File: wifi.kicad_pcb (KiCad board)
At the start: 4 copper layers, 58.4 x 69.6 mm, 134 parts, among them J1 Conn_02x10_Odd_Even, J11 Conn_Coaxial, J12 Conn_02x05_Counter_Clockwise, J13 Conn_02x03_Odd_Even, J14 Conn_01x02, J15 Conn_01x02, J16 Conn_01x02, J2 Conn_02x10_Odd_Even, J21 Conn_02x04_Odd_Even, J22 Conn_01x03, J23 Conn_01x03, J24 Conn_01x02, J3 Conn_02x06_Odd_Even, J5 Conn_01x03, J6 Conn_01x03, J7 Conn_02x07_Odd_Even, J9 Conn_01x02, Q2 TP0610T, Q3 BSS138, Q4 BSS138, Q5 BSS138, SW2 SW_DIP_x01, SW3 SW_DIP_x01, U1 CC3220SM2ARGKT, U10 TMP100, U8 MX25R3235FM1IL0, U9 OPA4340UA, Y2 32.768kHz, Y3 Crystal_GND24_Small

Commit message: Fixes for Aisler
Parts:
- added FID1: Fiducial, Fiducial:Fiducial_0.5mm_Mask1mm, F.Cu at (127.4, 51.8)
- added FID2: Fiducial, Fiducial:Fiducial_0.5mm_Mask1mm, F.Cu at (132.3, 110.9)
- added FID3: Fiducial, Fiducial:Fiducial_0.5mm_Mask1mm, F.Cu at (82.7, 52.2)
- added R45: 0, Resistor_SMD:R_0402_1005Metric, F.Cu at (79.1, 93.8)
- added R75: 0, Resistor_SMD:R_0402_1005Metric, F.Cu at (79.2, 85.3)
- added R78: 0, Resistor_SMD:R_0402_1005Metric, F.Cu at (131.3, 92.7)
- added R81: 0, Resistor_SMD:R_0402_1005Metric, F.Cu at (123.5, 95.2)
- added R85: 0, Resistor_SMD:R_0402_1005Metric, F.Cu at (123.6, 97.8)
- added R89: 0, Resistor_SMD:R_0402_1005Metric, F.Cu at (79.1, 95.5)
- added R91: 0, Resistor_SMD:R_0402_1005Metric, F.Cu at (79.1, 98.0)
- C35: footprint Capacitor_SMD:C_0402_1005Metric -> Capacitor_SMD:C_0603_1608Metric
- U1: footprint Package_DFN_QFN:Texas_S-PVQFN-N64_EP4.25x4.25mm -> Package_DFN_QFN:Texas_S-PVQFN-N64_EP4.25x4.25mm_ThermalVias
- moved J21 0.92 mm to (94.7, 54.9)
- moved J3 0.92 mm to (115.1, 54.9)
- moved J5 0.92 mm to (99.9, 57.4)
- moved J6 0.92 mm to (97.3, 57.4)
- moved R87 0.64 mm to (79.1, 92.3)
- moved C50 0.51 mm to (99.3, 95.8)
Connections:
- J1 pad 17: (no net) -> Net-(J1-Pad17)
- J1 pad 19: (no net) -> Net-(J1-Pad19)
- J1 pad 9: (no net) -> Net-(J1-Pad9)
- J2 pad 16: (no net) -> Net-(J2-Pad16)
- J2 pad 17: (no net) -> Net-(J2-Pad17)
- J2 pad 19: (no net) -> Net-(J2-Pad19)
- J2 pad 2: (no net) -> GND
- J3 pad 10: (no net) -> /P20_JTAG_TMS
- J3 pad 4: (no net) -> /P17_GPIO_24
- J3 pad 6: (no net) -> /P16_JTAG_TDI
- J3 pad 8: (no net) -> /P19_JTAG_TCK
- R52 pad 1: (no net) -> /P21_GPIO_25
- U1 pad 16: (no net) -> /P16_JTAG_TDI
- U1 pad 17: (no net) -> /P17_GPIO_24
- U1 pad 19: (no net) -> /P19_JTAG_TCK
- U1 pad 20: (no net) -> /P20_JTAG_TMS
- U1 pad 61: (no net) -> /P61_GPIO_06
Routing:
- net /P17_GPIO_24: track 0.00 -> 88.0 mm, vias 0 -> 4
- net /P16_JTAG_TDI: track 0.00 -> 77.1 mm, vias 0 -> 3
- net /P19_JTAG_TCK: track 0.00 -> 68.4 mm, vias 0 -> 2
- net /P20_JTAG_TMS: track 0.00 -> 68.3 mm, vias 0 -> 2
- net /P16_GPIO_23: track 0.00 -> 52.2 mm, vias 0 -> 2
- net /P61_GPIO_06: track 0.00 -> 35.4 mm, vias 0 -> 2
- net /P55_GPIO_01: track 56.3 -> 33.1 mm
- net /P21_GPIO_25: track 0.00 -> 16.0 mm, vias 0 -> 2
- net (no net): track 7.16 -> 0.00 mm, vias 1 -> 0
- net /ANA_IN2: track 31.9 -> 29.2 mm
- net Net-(J1-Pad19): track 0.00 -> 2.69 mm
- net Net-(J1-Pad17): track 0.00 -> 2.69 mm
- net Net-(J1-Pad9): track 0.00 -> 2.63 mm
- net /VBAT_CC: track 98.5 -> 100.9 mm, vias 8 -> 9
- net Net-(J2-Pad16): track 0.00 -> 2.31 mm
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- added copper zone on B.Cu, net GND
- added copper zone on P.Cu, net GND
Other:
- board text added: "5V"
- board text added: "BRD"
- board text added: "GND"
- board text added: "RST"
- board text added: "RX"
- board text added: "TCK"
- board text added: "TDI"
- board text added: "TDO"
- board text added: "TMS"
- board text added: "TX"
- board text added: "VBAT"
- board text added: "VS"

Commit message: MODASF initial commit
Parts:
- removed AE1: Antenna_Chip, pwrcon:Taiyo_WLAN
- removed the C27 at (113.0, 96.4)
- removed the C28 at (106.5, 77.2)
- removed the C29 at (113.3, 87.1)
- removed C32, C37, C38, C43, C44, C46, C47: 0.1uF, Capacitor_SMD:C_0402_1005Metric
- removed the C33 at (93.2, 81.8)
- removed the C34 at (109.2, 114.4)
- removed the C35 at (117.1, 90.4)
- removed C36: 10uF, Capacitor_SMD:C_0402_1005Metric
- removed C45: 10uF, Capacitor_SMD:C_0603_1608Metric
- removed C48, C49, C50, C51: 6.2pF, Capacitor_SMD:C_0402_1005Metric
- removed FL1: BFCN-2450, pwrcon:TDK_Filter
- removed J11: Conn_Coaxial, pwrcon:Co-axial_Connector_RF
- removed the J14 at (79.2, 58.2)
- removed the J21 at (94.7, 54.9)
- removed L3: L_Core_Ferrite_Small, Inductor_SMD:L_01005_0402Metric
- removed L4, L6: 2.2uH, Inductor_SMD:L_Wuerth_MAPI-2512
- removed L5: 1uH, Inductor_SMD:L_Wuerth_MAPI-2512
- removed R128, R39, R40, R43: 0, Resistor_SMD:R_0402_1005Metric
- removed R30: 1K, Resistor_SMD:R_0402_1005Metric
- removed R35: 10K, Resistor_SMD:R_0402_1005Metric
- removed R36: 0, Resistor_SMD:R_0603_1608Metric
- removed R41: 10k, Resistor_SMD:R_0402_1005Metric
- removed the R49 at (123.8, 67.8)
- removed the R50 at (122.0, 67.8)
- removed R51: 2.7K, Resistor_SMD:R_0402_1005Metric
- removed REF** (x4): MountingHole_2.1mm, MountingHole:MountingHole_2.1mm
- removed U8: MX25R3235FM1IL0, Package_SO:SOIC-8_3.9x4.9mm_P1.27mm
- removed Y2: 32.768kHz, Crystal:Crystal_SMD_3215-2Pin_3.2x1.5mm
- removed Y3: Crystal_GND24_Small, Crystal:Crystal_SMD_2520-4Pin_2.5x2.0mm
- added C41: 100uF, Capacitor_SMD:C_0402_1005Metric, F.Cu at (118.7, 72.9)
- added J10: Conn_01x02, Connector_PinHeader_2.54mm:PinHeader_1x02_P2.54mm_Vertical, F.Cu at (113.9, 105.6)
- added J16: Conn_01x02, Connector_PinHeader_2.54mm:PinHeader_1x02_P2.54mm_Vertical, F.Cu at (86.9, 54.9)
- added J17: Conn_01x02, Connector_PinHeader_2.54mm:PinHeader_1x02_P2.54mm_Vertical, F.Cu at (118.2, 54.9)
- added J18: Conn_01x02, Connector_PinHeader_2.54mm:PinHeader_1x02_P2.54mm_Vertical, F.Cu at (94.2, 54.9)
- added J19: Conn_01x02, Connector_PinHeader_2.54mm:PinHeader_1x02_P2.54mm_Vertical, F.Cu at (91.9, 54.9)
- added J20: Conn_01x02, Connector_PinHeader_2.54mm:PinHeader_1x02_P2.54mm_Vertical, F.Cu at (89.5, 54.9)
- added J22: Conn_01x03, Connector_PinHeader_2.54mm:PinHeader_1x03_P2.54mm_Vertical, F.Cu at (84.9, 110.4)
- added R104: 0, Resistor_SMD:R_0402_1005Metric, F.Cu at (88.1, 99.5)
- added R31: 1K, Resistor_SMD:R_0402_1005Metric, F.Cu at (111.6, 69.0)
- added R42: 0, Resistor_SMD:R_0402_1005Metric, F.Cu at (131.1, 77.7)
- added R46: 0, Resistor_SMD:R_0402_1005Metric, F.Cu at (131.1, 82.2)
- added R52: 0, Resistor_SMD:R_0402_1005Metric, F.Cu at (131.6, 87.6)
- added R56: 0, Resistor_SMD:R_0402_1005Metric, F.Cu at (131.5, 90.2)
- added R65: 0, Resistor_SMD:R_0402_1005Metric, F.Cu at (79.0, 90.4)
- added TP1: TestPoint, TestPoint:TestPoint_Pad_D2.0mm, F.Cu at (115.2, 69.0)
- C33: renamed from C30; value 4.7uF -> 0.1uF
- C34: renamed from C31; value 4.7uF -> 0.1uF
- C42: value 10uF -> 100uF; footprint Capacitor_SMD:C_0603_1608Metric -> Capacitor_SMD:C_0402_1005Metric
- R119: value 3.3K -> 0
- R126: renamed from R118; value 3.3K -> 0
- R145: renamed from R147; value 270 -> 750
- R146: renamed from R148; value 270 -> 750
- R147: renamed from R149; value 270 -> 750
- U1: value CC3220SM2ARGKT -> CC3220MODASF12MONR; footprint Package_DFN_QFN:Texas_S-PVQFN-N64_EP4.25x4.25mm_ThermalVias -> TIMOD_footprints:CC3220MODASF12MONR
- U10: value TMP100 -> TMP006AIYZFR; footprint Package_TO_SOT_SMD:SOT-23-6 -> TMP006_footprints:TMP006AIYZFR
- moved J9 63.3 mm to (79.0, 57.4)
- moved J26 40.0 mm to (121.7, 116.2), turned to 270 degrees
- moved J14 38.4 mm to (116.7, 78.6), turned to 225 degrees
- moved J15 38.2 mm to (112.3, 74.2), turned to 225 degrees
- moved R126 33.1 mm to (109.6, 84.9), turned to 180 degrees
- moved R119 32.8 mm to (106.4, 82.6), turned to 180 degrees
- moved R44 31.5 mm to (131.1, 80.0), turned to 0 degrees
- moved R121 30.9 mm to (113.7, 79.6), turned to 0 degrees
- moved R127 30.3 mm to (107.6, 73.5), turned to 180 degrees
- moved C35 30.0 mm to (106.4, 88.1)
- moved R114 29.9 mm to (107.6, 88.1)
- moved U10 29.4 mm to (106.4, 85.3), turned to 180 degrees
- moved C34 27.2 mm to (115.2, 108.8), turned to 270 degrees
- moved C33 23.1 mm to (113.5, 108.8), turned to 270 degrees
- moved R133 22.9 mm to (103.2, 87.9)
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- renumbered C52 to C26, C53 to C27, C54 to C28, C55 to C29, C56 to C30, C57 to C35, D8 to D7, J12 to J112, J13 to J12, J15 to J14, J16 to J15, J22 to J21, J23 to J26, Q3 to Q4, Q2 to Q5, Q4 to Q6, Q5 to Q7, R45 to R105, R47 to R107, R52 to R109, R53 to R113, R116 to R114, R123 to R121, R129 to R127, R134 to R132, R135 to R133, R136 to R134, R138 to R136, R139 to R137, R141 to R139, R142 to R140, R151 to R149, R152 to R150, R153 to R151, R154 to R152, R57 to R38, R67 to R49, R68 to R50, R71 to R53, R72 to R54, R75 to R57, R76 to R58, R78 to R60, R80 to R62, R81 to R63, R82 to R64, R84 to R66, R85 to R67, R86 to R68, R87 to R69, R88 to R70, R89 to R71, R90 to R72, R91 to R73, R92 to R74, R102 to R84, R103 to R85, R104 to R86, R105 to R87, R106 to R88, R107 to R89, R110 to R92, R111 to R93, R112 to R94, R113 to R95, R114 to R96, R115 to R97
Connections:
- net Net-(J1-Pad5) renamed /RX
- net Net-(J1-Pad7) renamed /TX
- net Net-(J1-Pad9) renamed /GPIO
- C35 pad 2: Net-(C57-Pad2) -> Net-(C35-Pad2)
- C42 pad 2: /VDD_DIG_CC -> /VBAT_CC
- J1 pad 1: Net-(J1-Pad1) -> /PWR
- J1 pad 13: (no net) -> Net-(J1-Pad13)
- J112 pad 10: /SFL_CS -> (no net)
- J112 pad 6: /SFL_DIN -> (no net)
- J112 pad 7: /SFL_DOUT -> (no net)
- J112 pad 8: /SFL_CLK -> (no net)
- J12 pad 1: Net-(J13-Pad1) -> Net-(J12-Pad1)
- J12 pad 3: Net-(J13-Pad1) -> Net-(J12-Pad1)
- J12 pad 5: Net-(J13-Pad1) -> Net-(J12-Pad1)
- J2 pad 12: (no net) -> Net-(J2-Pad12)
- J2 pad 14: (no net) -> Net-(J2-Pad14)
- J2 pad 4: (no net) -> Net-(J2-Pad4)
- J2 pad 6: (no net) -> Net-(J2-Pad6)
- J2 pad 8: (no net) -> Net-(J2-Pad8)
- J26 pad 1: /VCC_5V -> /VCC_BRD
- J26 pad 2: GND -> Net-(J26-Pad2)
- J26 pad 3: GND -> /VBAT_CC
- J3 pad 4: /P17_GPIO_24 -> /P17_JTAG_TDO
- J9 pad 1: Net-(J9-Pad1) -> /VCC_BRD
- J9 pad 2: /VBAT_CC -> /VCC_OPAMP
- R105 pad 1: /P16_GPIO_23 -> /P16_JTAG_TDI
- R105 pad 2: /P16_JTAG_TDI -> /P16_GPIO_23
- R107 pad 1: /VCC_BRD -> Net-(J12-Pad1)
- R107 pad 2: Net-(J13-Pad1) -> Net-(J26-Pad2)
- R114 pad 1: /VCC_BRD -> (no net)
- R114 pad 2: Net-(C57-Pad2) -> Net-(C35-Pad2)
- R119 pad 1: /VCC_BRD -> Net-(R119-Pad1)
- R119 pad 2: /SENS_I2C_SCL -> /VCC_BRD
- R126 pad 1: /SENS_I2C_SDA -> GND
- R126 pad 2: /VCC_BRD -> Net-(R126-Pad2)
- R132 pad 1: Net-(R134-Pad1) -> (no net)
- R132 pad 2: /SENS_I2C_SCL -> (no net)
- R133 pad 1: Net-(R135-Pad1) -> (no net)
- R133 pad 2: /SENS_I2C_SDA -> (no net)
- R38 pad 1: /VCC_BRD -> /PWR
- R38 pad 2: Net-(J1-Pad1) -> /VBAT_CC
- R44 pad 1: Net-(R44-Pad1) -> /P08_GPIO_17
- R44 pad 2: GND -> Net-(J2-Pad6)
- U1 pad 1: /P01_GPIO_10 -> GND
- U1 pad 10: Net-(C28-Pad1) -> /P04_GPIO_13
- U1 pad 11: /SFL_CLK -> /P15_GPIO_22
- U1 pad 12: /SFL_DOUT -> /P16_JTAG_TDI
- U1 pad 13: /SFL_DIN -> (no net)
- U1 pad 14: /SFL_CS -> (no net)
- U1 pad 15: /P15_GPIO_22 -> (no net)
- U1 pad 16: /P16_JTAG_TDI -> GND
- U1 pad 17: /P17_GPIO_24 -> (no net)
- U1 pad 18: (no net) -> /P17_JTAG_TDO
- U1 pad 19: /P19_JTAG_TCK -> /P18_GPIO_28
- U1 pad 2: /P02_GPIO_11 -> GND
- U1 pad 20: /P20_JTAG_TMS -> (no net)
- U1 pad 21: /SOP2 -> /P19_JTAG_TCK
- U1 pad 22: Net-(C50-Pad1) -> /P20_JTAG_TMS
- U1 pad 23: Net-(R44-Pad1) -> /SOP2
- U1 pad 24: /VDD_PL -> /SOP1
- U1 pad 25: /LDO_IN -> (no net)
- U1 pad 27: (no net) -> GND
- U1 pad 28: (no net) -> GND
- U1 pad 3: /P03_GPIO_12 -> /P01_GPIO_10
- U1 pad 30: (no net) -> GND
- U1 pad 31: Net-(FL1-Pad1) -> (no net)
- U1 pad 32: /CC_nRESET -> GND
- U1 pad 34: /SOP1 -> /SOP0
- U1 pad 35: /SOP0 -> (no net)
- U1 pad 36: /LDO_IN -> Net-(J10-Pad1)
- U1 pad 38: Net-(L4-Pad2) -> GND
- U1 pad 39: /VBAT_CC -> (no net)
- U1 pad 4: /P04_GPIO_13 -> /P02_GPIO_11
- U1 pad 40: Net-(L5-Pad1) -> /VBAT_CC
- U1 pad 41: Net-(L5-Pad2) -> (no net)
- U1 pad 42: (no net) -> /P53_GPIO_30
- U1 pad 43: Net-(L6-Pad1) -> GND
- U1 pad 44: /VBAT_CC -> /P50_GPIO_00
- U1 pad 46: (no net) -> /P55_GPIO_01
- U1 pad 47: /VDD_FL -> /P57_GPIO_02
- U1 pad 48: /LDO_IN -> /P58_GPIO_03
- U1 pad 49: Net-(C46-Pad1) -> /P59_GPIO_04
- U1 pad 5: (no net) -> /P05_GPIO_14
- U1 pad 50: /P50_GPIO_00 -> /P60_GPIO_05
- U1 pad 51: Net-(C49-Pad2) -> /P61_GPIO_06
- U1 pad 52: Net-(C48-Pad2) -> /P62_GPIO_07
- U1 pad 53: /P53_GPIO_30 -> /P63_GPIO_08
- U1 pad 54: Net-(C28-Pad1) -> /P64_GPIO_09
- U1 pad 55: /P55_GPIO_01 -> GND
- U1 pad 56: /VDD_DIG_CC -> GND
- U1 pad 57: /P57_GPIO_02 -> GND
- U1 pad 58: /P58_GPIO_03 -> GND
- U1 pad 59: /P59_GPIO_04 -> GND
- U1 pad 6: (no net) -> /P06_GPIO_15
- U1 pad 60: /P60_GPIO_05 -> GND
- U1 pad 61: /P61_GPIO_06 -> GND
- U1 pad 62: /P62_GPIO_07 -> GND
- U1 pad 63: /P63_GPIO_08 -> GND
- U1 pad 7: (no net) -> /P07_GPIO_16
- U1 pad 8: (no net) -> /P08_GPIO_17
- U1 pad 9: /VDD_DIG_CC -> /P03_GPIO_12
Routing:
- net /VCC_BRD: track 196.3 -> 37.5 mm, vias 10 -> 6
- net /P01_GPIO_10: track 125.4 -> 1.86 mm, vias 7 -> 0
- net /P02_GPIO_11: track 119.9 -> 1.99 mm, vias 7 -> 0
- net /VBAT_CC: track 100.9 -> 6.39 mm, vias 9 -> 1
- net /P17_GPIO_24: track 88.0 -> 0.28 mm, vias 4 -> 0
- net /P64_GPIO_09: track 81.0 -> 3.19 mm, vias 3 -> 1
- net /P50_GPIO_00: track 77.1 -> 0.00 mm, vias 5 -> 0
- net /P16_JTAG_TDI: track 77.1 -> 0.44 mm, vias 3 -> 0
- net /P19_JTAG_TCK: track 68.4 -> 0.00 mm, vias 2 -> 0
- net /P20_JTAG_TMS: track 68.3 -> 0.00 mm, vias 2 -> 0
- net GND: track 80.6 -> 16.0 mm, vias 38 -> 4
- net /VCC_5V: track 62.8 -> 0.00 mm
- net /SOP2: track 62.1 -> 0.00 mm, vias 2 -> 0
- net /CC_nRESET: track 104.1 -> 49.5 mm, vias 4 -> 2
- net /P16_GPIO_23: track 52.2 -> 1.09 mm, vias 2 -> 1
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- removed copper zone on P.Cu, net /LDO_IN
- removed copper zone on P.Cu, net /VBAT_CC
- removed copper zone on P.Cu, net /VCC_BRD
- removed copper zone on B.Cu, net GND
- removed copper zone on F.Cu, net GND
- removed copper zone on G.Cu, net GND
- removed copper zone on P.Cu, net GND

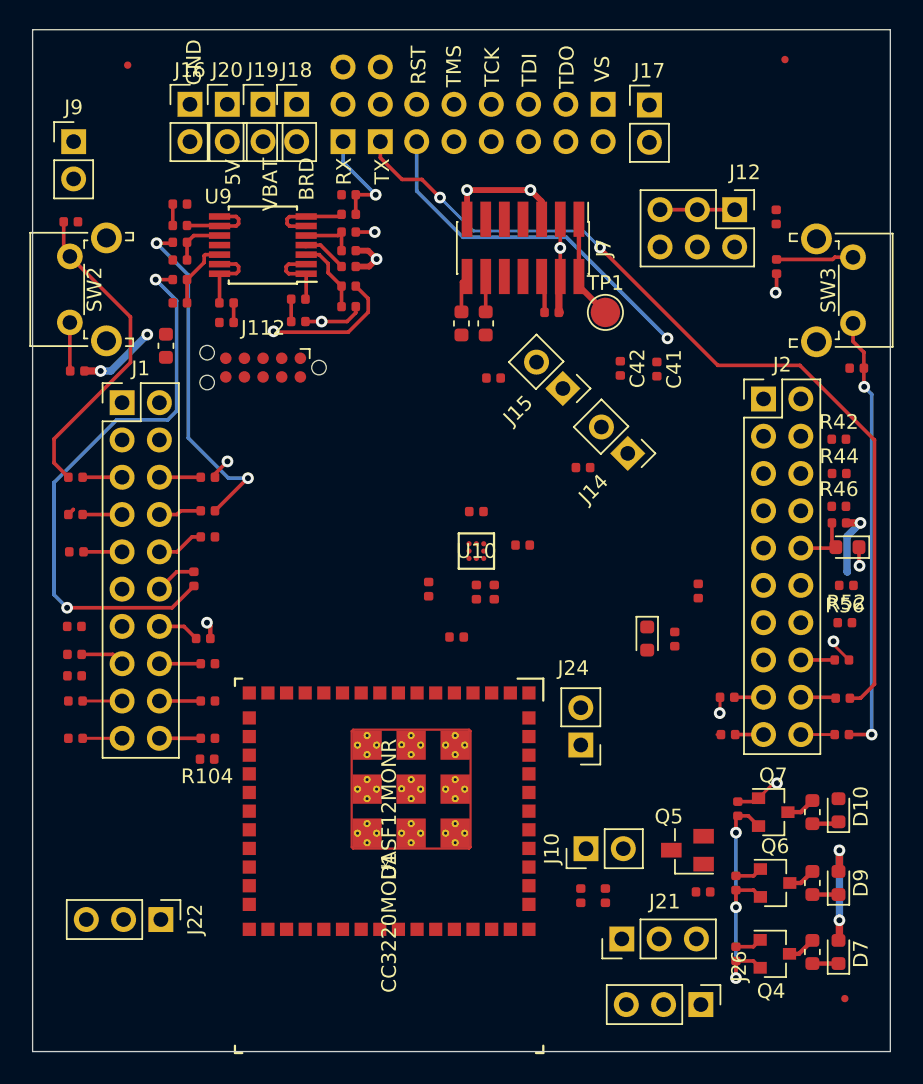
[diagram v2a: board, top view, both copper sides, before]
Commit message: Updated BoM, decided to use 3 LEDs and switches from cc3220s layout
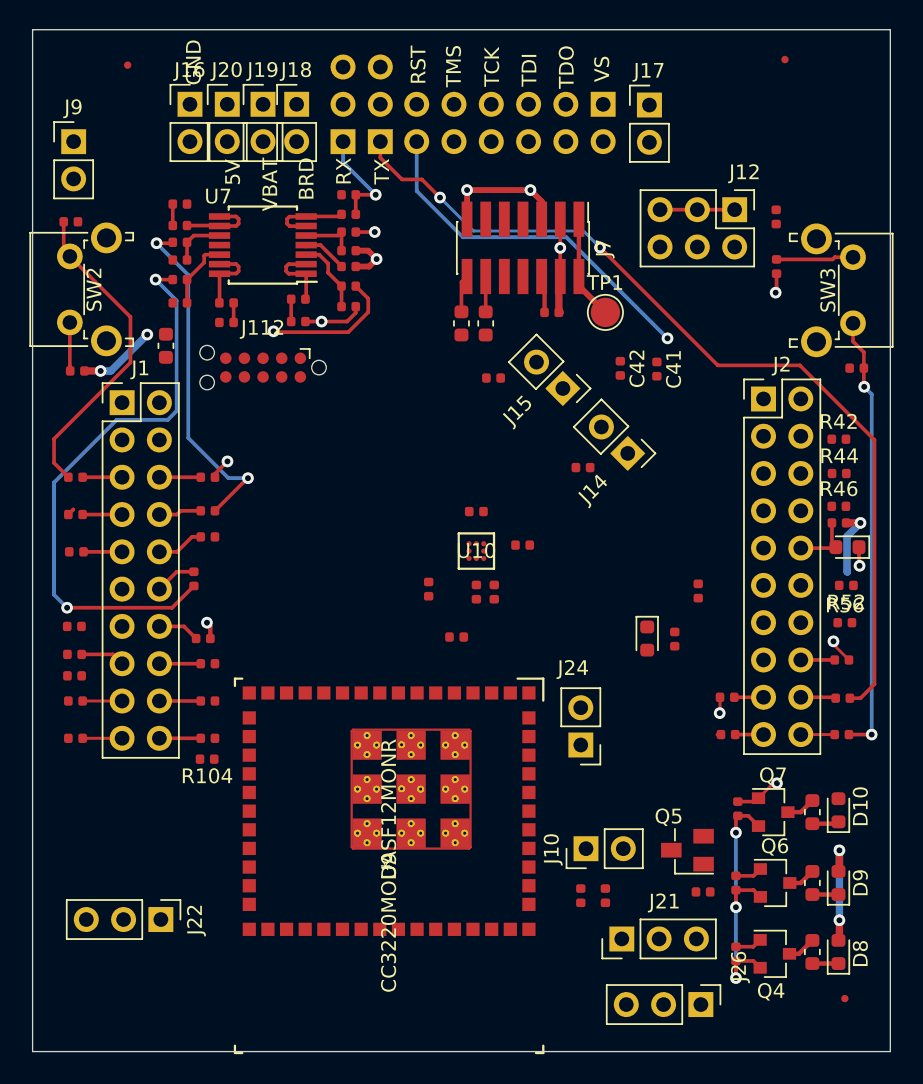
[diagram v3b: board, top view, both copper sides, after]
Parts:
- R145, R146, R147: value 750 -> 270
- renumbered D7 to D8, U9 to U7, U1 to U9
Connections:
- R114 pad 1: (no net) -> /VCC_BRD
- R132 pad 1: (no net) -> Net-(R132-Pad1)
- R132 pad 2: (no net) -> /SENS_I2C_SCL
- R133 pad 1: (no net) -> /SENS_I2C_SDA
- R133 pad 2: (no net) -> Net-(R133-Pad2)
- U10 pad B3: /SENS_I2C_SDA -> Net-(R132-Pad1)
- U10 pad C3: /SENS_I2C_SCL -> Net-(R133-Pad2)

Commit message: Smaller board size, removed SW3
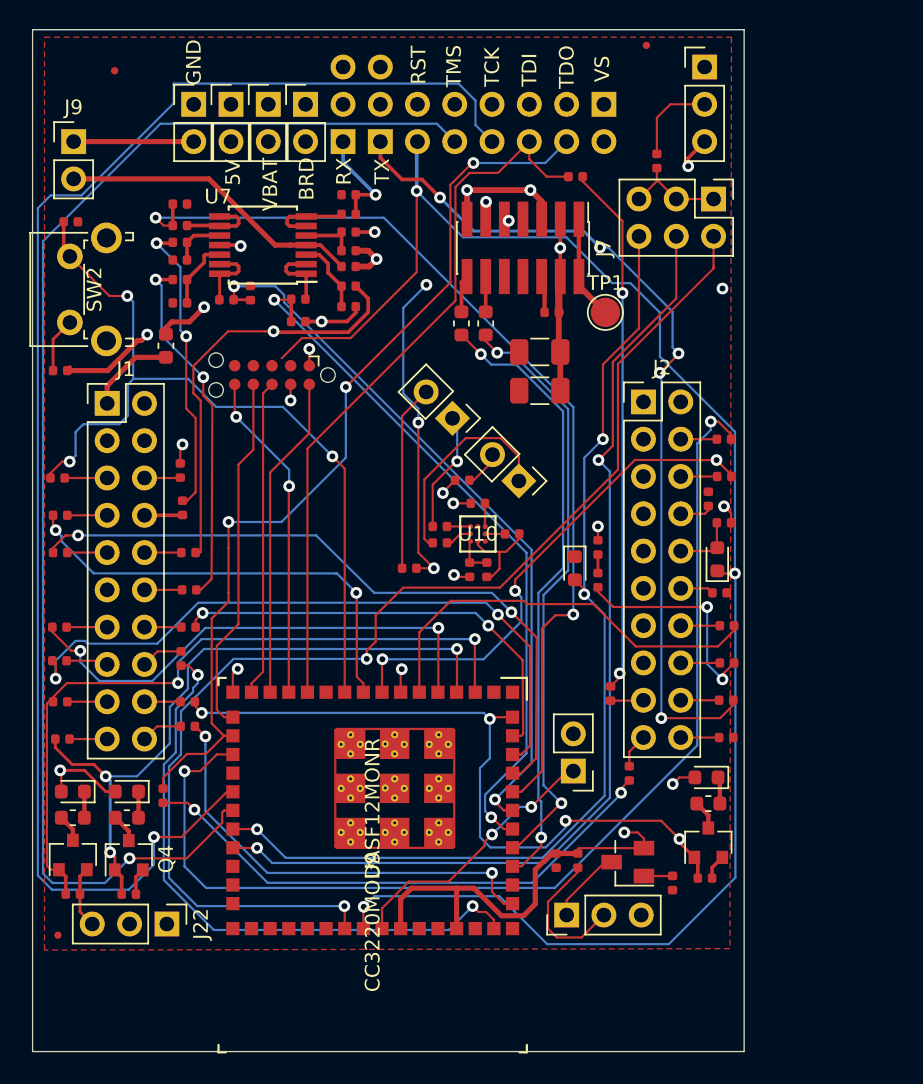
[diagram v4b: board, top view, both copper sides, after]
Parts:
- removed J17, J24: Conn_01x02, Connector_PinHeader_2.54mm:PinHeader_1x02_P2.54mm_Vertical
- removed R137: 1K, Resistor_SMD:R_0402_1005Metric
- removed R140: 10K, Resistor_SMD:R_0402_1005Metric
- removed SW3: SW_DIP_x01, Button_Switch_THT:SW_Tactile_SPST_Angled_PTS645Vx31-2LFS
- C41, C42: footprint Capacitor_SMD:C_0402_1005Metric -> Capacitor_SMD:C_1206_3216Metric
- moved J26 63.9 mm to (122.0, 52.3), turned to 0 degrees
- moved FID2 53.8 mm to (77.9, 111.5)
- moved D9 52.5 mm to (78.9, 101.7), turned to 180 degrees
- moved R145 50.6 mm to (78.9, 103.5), turned to 180 degrees
- moved D8 49.7 mm to (82.6, 101.7), turned to 180 degrees
- moved R105 48.2 mm to (113.2, 59.8)
- moved Q6 47.9 mm to (78.9, 106.0), turned to 90 degrees
- moved R146 47.6 mm to (82.6, 103.5), turned to 180 degrees
- moved R150 45.2 mm to (78.9, 108.7), turned to 0 degrees
- moved Q4 44.5 mm to (82.8, 106.0), turned to 90 degrees
- moved R149 41.6 mm to (82.8, 108.7), turned to 0 degrees
- moved R127 14.2 mm to (101.9, 86.5), turned to 0 degrees
- moved FID1 9.49 mm to (118.0, 50.9)
- moved D10 9.27 mm to (122.1, 100.7), turned to 180 degrees
- moved R107 8.98 mm to (118.7, 58.7), turned to 90 degrees
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- renumbered J112 to J13
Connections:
- J13 pad 10: (no net) -> /SPI_CS_IN
- J13 pad 6: (no net) -> /SPI_MISO
- J13 pad 7: (no net) -> /SPI_MOSI
- J13 pad 8: (no net) -> /SPI_CLK
- J3 pad 2: (no net) -> /VCC_BRD
- Q4 pad 2: Net-(J24-Pad1) -> GND
- Q6 pad 2: Net-(J24-Pad1) -> GND
- Q7 pad 2: Net-(J24-Pad1) -> GND
- R149 pad 2: Net-(J24-Pad1) -> GND
- R150 pad 2: Net-(J24-Pad1) -> GND
- R151 pad 2: Net-(J24-Pad1) -> GND
- R52 pad 1: /P07_GPIO_16 -> (no net)
- R68 pad 1: /P15_GPIO_22 -> (no net)
- U9 pad 11: /P15_GPIO_22 -> (no net)
- U9 pad 13: (no net) -> /SPI_MISO
- U9 pad 14: (no net) -> /SPI_CS_IN
- U9 pad 15: (no net) -> /SPI_CLK
- U9 pad 17: (no net) -> /SPI_MOSI
- U9 pad 35: (no net) -> /CC_nRESET
- U9 pad 7: /P07_GPIO_16 -> (no net)
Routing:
- net /P19_JTAG_TCK: track 0.00 -> 100.9 mm, vias 0 -> 1
- net /P20_JTAG_TMS: track 0.00 -> 90.6 mm, vias 0 -> 1
- net /SOP0: track 0.00 -> 82.6 mm, vias 0 -> 2
- net /P01_GPIO_10: track 1.86 -> 82.8 mm, vias 0 -> 4
- net /P02_GPIO_11: track 1.99 -> 82.9 mm, vias 0 -> 7
- net /P18_GPIO_28: track 0.00 -> 74.3 mm, vias 0 -> 2
- net /SOP2: track 0.00 -> 69.4 mm, vias 0 -> 3
- net /SOP1: track 0.00 -> 68.7 mm, vias 0 -> 2
- net /P60_GPIO_05: track 1.55 -> 65.7 mm, vias 0 -> 2
- net /CC_nRESET: track 49.5 -> 112.7 mm, vias 2 -> 3
- net /P17_JTAG_TDO: track 0.00 -> 62.5 mm, vias 0 -> 3
- net /VCC_5V: track 0.00 -> 57.6 mm
- net /VBAT_CC: track 6.39 -> 56.6 mm, vias 1 -> 4
- net /P16_JTAG_TDI: track 0.44 -> 49.7 mm
- net /P59_GPIO_04: track 1.36 -> 49.7 mm, vias 0 -> 2
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- added copper zone on P.Cu, net /VBAT_CC
- added copper zone on P.Cu, net /VCC_BRD
- added copper zone on F.Cu, net GND
- added copper zone on G.Cu, net GND
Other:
- board size 58.4 x 69.6 mm -> 48.5 x 69.6 mm
